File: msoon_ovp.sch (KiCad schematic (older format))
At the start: 7 parts, among them J1 Conn_01x02, U1 LM285M-ADJ

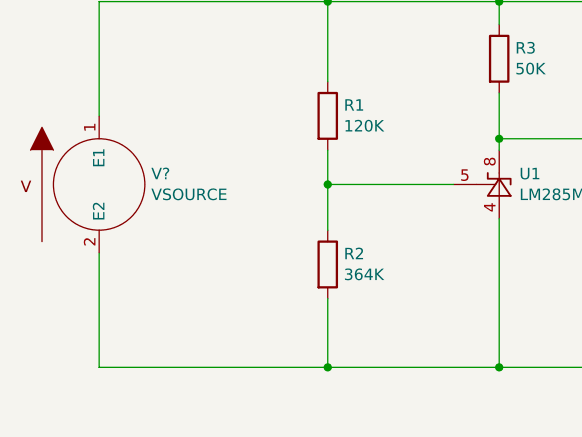
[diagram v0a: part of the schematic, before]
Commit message: Annotate and add tran directive to schematic
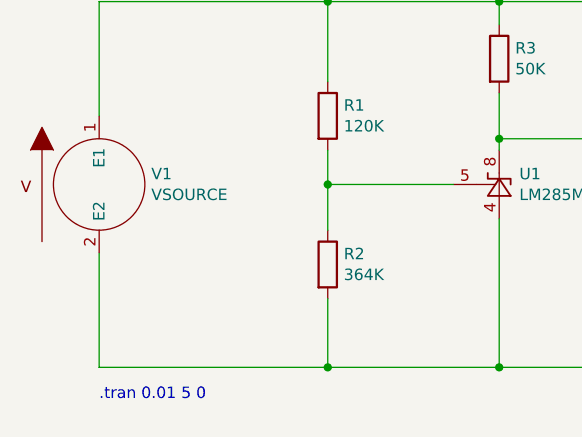
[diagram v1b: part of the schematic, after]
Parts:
- gave numbers to parts that had none: 1
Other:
- note added: ".tran 0.01 5 0"
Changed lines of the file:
@@
 	6650 3500 6650 4250
 $Comp
-L pspice:VSOURCE V?
+L pspice:VSOURCE V1
 U 1 1 5F7060C9
 P 3100 3450
-F 0 "V?" H 3328 3496 50  0000 L CNN
+F 0 "V1" H 3328 3496 50  0000 L CNN
 F 1 "VSOURCE" H 3328 3405 50  0000 L CNN
 F 2 "" H 3100 3450 50  0001 C CNN
@@
 Wire Wire Line
 	3100 4250 4100 4250
+Text Notes 3100 4400 0    50   ~ 0
+.tran 0.01 5 0
 $EndSCHEMATC

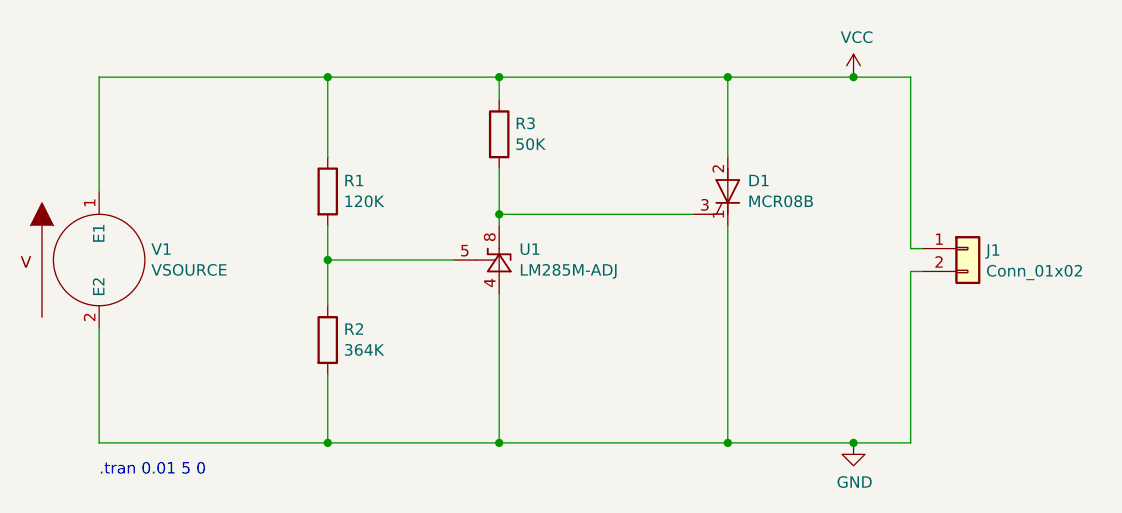
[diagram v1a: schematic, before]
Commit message: Something, dunno what
... does not matter much, we will discard this and just add zers instead
of a fancy crowbar.
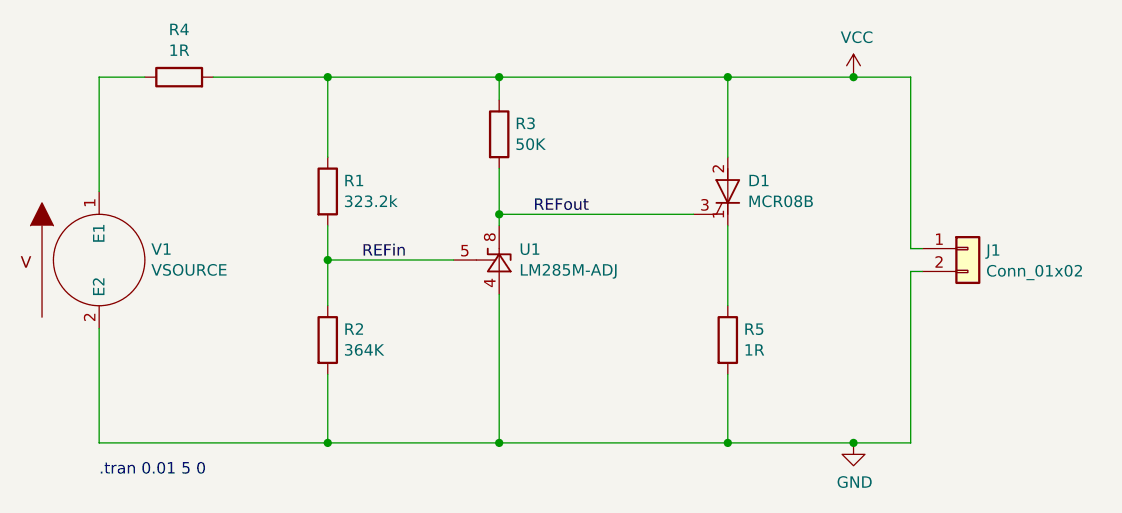
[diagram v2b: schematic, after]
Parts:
- added R4, R5: 1R, Resistor_SMD:R_0805_2012Metric, symbol Device:R
- R1: value 120K -> 323.2k
- U1: Spice_Lib_File spice_models/LM385-ADJ_TRANS.LIB -> spice_models/TL431LI_AVG.LIB; Spice_Model LM385-ADJ_TRANS -> TL431LI_AVG; Spice_Node_Sequence 4 5 8 1 2 3 6 7 -> 8 5 4
- V1: Spice_Model pulse(0 15 1 1 1) -> pulse(0 15 1 1 1 1)
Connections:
- net GND: now also R5.2; no longer D1.1 (K)
- net VCC: now also R4.2; no longer V1.1 (E1)
- net REFin: now reaches R1.2, R2.1, U1.5 (FB)
- net REFout: now reaches D1.3 (G), R3.2, U1.8 (K)
- new net: D1.1 (K), R5.1
- new net: R4.1, V1.1 (E1)
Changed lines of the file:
@@
 F 3 "http://www.ti.com/lit/ds/symlink/lm185-adj.pdf" H 4850 3450 50  0001 C CIN
 F 4 "X" H 4850 3450 50  0001 C CNN "Spice_Primitive"
-F 5 "LM385-ADJ_TRANS" H 4850 3450 50  0001 C CNN "Spice_Model"
+F 5 "TL431LI_AVG" H 4850 3450 50  0001 C CNN "Spice_Model"
 F 6 "Y" H 4850 3450 50  0001 C CNN "Spice_Netlist_Enabled"
-F 7 "4 5 8 1 2 3 6 7" H 4850 3450 50  0001 C CNN "Spice_Node_Sequence"
-F 8 "spice_models/LM385-ADJ_TRANS.LIB" H 4850 3450 50  0001 C CNN "Spice_Lib_File"
+F 7 "8 5 4" H 4850 3450 50  0001 C CNN "Spice_Node_Sequence"
+F 8 "spice_models/TL431LI_AVG.LIB" H 4850 3450 50  0001 C CNN "Spice_Lib_File"
 	1    4850 3450
 	0    -1   -1   0
@@
 P 4100 3150
 F 0 "R1" H 4170 3196 50  0000 L CNN
-F 1 "120K" H 4170 3105 50  0000 L CNN
+F 1 "323.2k" H 4170 3105 50  0000 L CNN
 F 2 "Resistor_SMD:R_0805_2012Metric" V 4030 3150 50  0001 C CNN
 F 3 "~" H 4100 3150 50  0001 C CNN
@@
 Connection ~ 5850 2650
 Wire Wire Line
-	5850 3300 5850 4250
+	5850 3300 5850 3650
 Connection ~ 5850 4250
 Wire Wire Line
@@
 F 3 "~" H 3100 3450 50  0001 C CNN
 F 4 "V" H 3100 3450 50  0001 C CNN "Spice_Primitive"
-F 5 "pulse(0 15 1 1 1)" H 3100 3450 50  0001 C CNN "Spice_Model"
+F 5 "pulse(0 15 1 1 1 1)" H 3100 3450 50  0001 C CNN "Spice_Model"
 F 6 "Y" H 3100 3450 50  0001 C CNN "Spice_Netlist_Enabled"
 	1    3100 3450
@@
 	3100 3150 3100 2650
 Wire Wire Line
-	3100 2650 4100 2650
+	3100 2650 3300 2650
 Wire Wire Line
 	3100 3750 3100 4250
 Wire Wire Line
 	3100 4250 4100 4250
+Text Label 5000 3250 0    50   ~ 0
+REFout
+Text Label 4250 3450 0    50   ~ 0
+REFin
+$Comp
+L Device:R R4
+U 1 1 5F70E79C
+P 3450 2650
+F 0 "R4" V 3657 2650 50  0000 C CNN
+F 1 "1R" V 3566 2650 50  0000 C CNN
+F 2 "Resistor_SMD:R_0805_2012Metric" V 3380 2650 50  0001 C CNN
+F 3 "~" H 3450 2650 50  0001 C CNN
+	1    3450 2650
+	0    -1   -1   0
+$EndComp
+Wire Wire Line
+	3600 2650 4100 2650
+$Comp
+L Device:R R5
+U 1 1 5F710067
+P 5850 3800
+F 0 "R5" H 5920 3846 50  0000 L CNN
+F 1 "1R" H 5920 3755 50  0000 L CNN
+F 2 "Resistor_SMD:R_0805_2012Metric" V 5780 3800 50  0001 C CNN
+F 3 "~" H 5850 3800 50  0001 C CNN
+F 4 "R" H 5850 3800 50  0001 C CNN "Spice_Primitive"
+F 5 "1" H 5850 3800 50  0001 C CNN "Spice_Model"
+F 6 "Y" H 5850 3800 50  0001 C CNN "Spice_Netlist_Enabled"
+	1    5850 3800
+	1    0    0    -1
+$EndComp
+Wire Wire Line
+	5850 3950 5850 4250
 Text Notes 3100 4400 0    50   ~ 0
 .tran 0.01 5 0
